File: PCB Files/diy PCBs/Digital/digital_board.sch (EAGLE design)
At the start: 18 parts

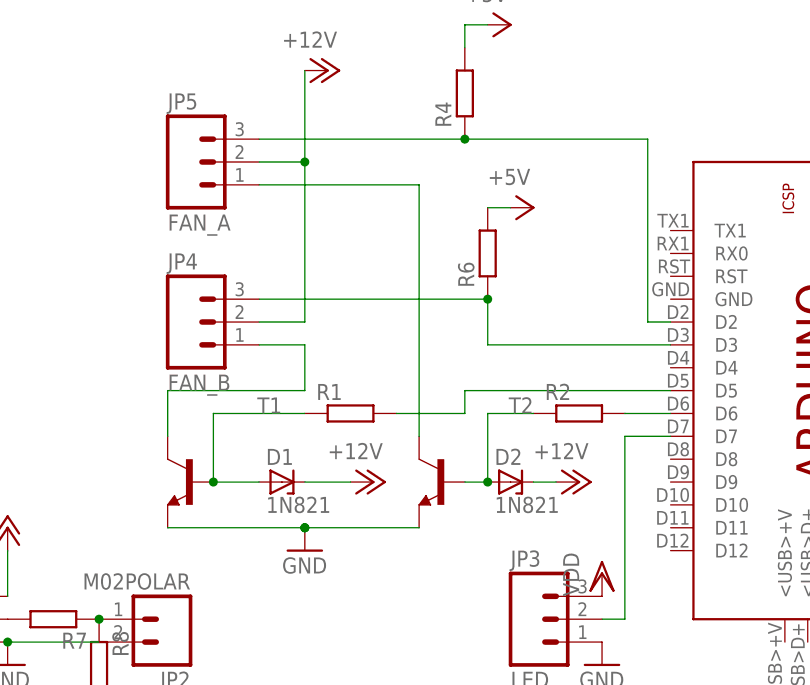
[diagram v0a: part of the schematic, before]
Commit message: made fixed a small bug and changed diode parameters
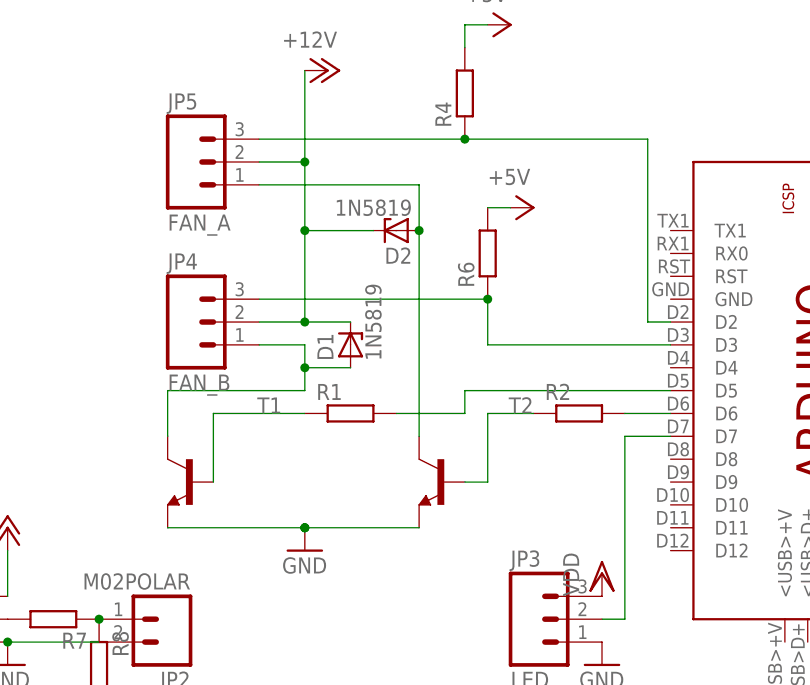
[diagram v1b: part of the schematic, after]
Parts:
- D1, D2: value 1N821 -> 1N5819
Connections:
- removed net N$6: D2.A, R2.1, T2.B
- new net N$2: R2.1
- net N$3: now also D1.A
- net N$4: now also D2.A
- net N$5: no longer D1.A
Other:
- moved on the sheet: D1, D2
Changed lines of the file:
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@@
 <part name="VDD1" library="supply1" deviceset="VDD" device=""/>
 <part name="VDD2" library="supply1" deviceset="VDD" device=""/>
-<part name="D1" library="diode" deviceset="1N821" device=""/>
-<part name="D2" library="diode" deviceset="1N821" device=""/>
-<part name="P+4" library="supply1" deviceset="+12V" device=""/>
-<part name="P+6" library="supply1" deviceset="+12V" device=""/>
+<part name="D1" library="diode" deviceset="1N821" device="" value="1N5819"/>
+<part name="D2" library="diode" deviceset="1N821" device="" value="1N5819"/>
 </parts>
 <sheets>
@@
 <instance part="VDD1" gate="G$1" x="0" y="25.4"/>
 <instance part="VDD2" gate="G$1" x="-27.94" y="-7.62" rot="R180"/>
-<instance part="D1" gate="1" x="-35.56" y="35.56"/>
-<instance part="D2" gate="1" x="-10.16" y="35.56"/>
-<instance part="P+4" gate="1" x="-25.4" y="35.56" rot="R270"/>
-<instance part="P+6" gate="1" x="-2.54" y="35.56" rot="R270"/>
+<instance part="D1" gate="1" x="-27.94" y="50.8" rot="R90"/>
+<instance part="D2" gate="1" x="-22.86" y="63.5" rot="R180"/>
 </instances>
 <busses>
@@
 <pinref part="T1" gate="G$1" pin="C"/>
 <wire x1="-38.1" y1="50.8" x2="-33.02" y2="50.8" width="0.1524" layer="91"/>
-<wire x1="-33.02" y1="50.8" x2="-33.02" y2="45.72" width="0.1524" layer="91"/>
+<wire x1="-33.02" y1="50.8" x2="-33.02" y2="48.26" width="0.1524" layer="91"/>
+<wire x1="-33.02" y1="48.26" x2="-33.02" y2="45.72" width="0.1524" layer="91"/>
 <wire x1="-33.02" y1="45.72" x2="-48.26" y2="45.72" width="0.1524" layer="91"/>
 <wire x1="-48.26" y1="45.72" x2="-48.26" y2="40.64" width="0.1524" layer="91"/>
+<pinref part="D1" gate="1" pin="A"/>
+<wire x1="-27.94" y1="48.26" x2="-33.02" y2="48.26" width="0.1524" layer="91"/>
+<junction x="-33.02" y="48.26"/>
 </segment>
 </net>
@@
 <pinref part="T2" gate="G$1" pin="C"/>
 <wire x1="-38.1" y1="68.58" x2="-20.32" y2="68.58" width="0.1524" layer="91"/>
-<wire x1="-20.32" y1="68.58" x2="-20.32" y2="40.64" width="0.1524" layer="91"/>
+<wire x1="-20.32" y1="68.58" x2="-20.32" y2="63.5" width="0.1524" layer="91"/>
+<pinref part="D2" gate="1" pin="A"/>
+<wire x1="-20.32" y1="63.5" x2="-20.32" y2="40.64" width="0.1524" layer="91"/>
+<junction x="-20.32" y="63.5"/>
 </segment>
 </net>
 <net name="+12V" class="0">
 <segment>
-<wire x1="-33.02" y1="53.34" x2="-33.02" y2="71.12" width="0.1524" layer="91"/>
+<wire x1="-33.02" y1="53.34" x2="-33.02" y2="63.5" width="0.1524" layer="91"/>
 <pinref part="P+1" gate="1" pin="+12V"/>
 <pinref part="JP5" gate="G$1" pin="2"/>
+<wire x1="-33.02" y1="63.5" x2="-33.02" y2="71.12" width="0.1524" layer="91"/>
 <wire x1="-33.02" y1="71.12" x2="-33.02" y2="81.28" width="0.1524" layer="91"/>
 <wire x1="-38.1" y1="71.12" x2="-33.02" y2="71.12" width="0.1524" layer="91"/>
@@
 <pinref part="JP4" gate="G$1" pin="2"/>
 <wire x1="-33.02" y1="53.34" x2="-38.1" y2="53.34" width="0.1524" layer="91"/>
+<pinref part="D1" gate="1" pin="C"/>
+<wire x1="-27.94" y1="53.34" x2="-33.02" y2="53.34" width="0.1524" layer="91"/>
+<pinref part="D2" gate="1" pin="C"/>
+<wire x1="-25.4" y1="63.5" x2="-33.02" y2="63.5" width="0.1524" layer="91"/>
+<junction x="-33.02" y="63.5"/>
+<junction x="-33.02" y="53.34"/>
 </segment>
 <segment>
@@
 <pinref part="JP6" gate="G$1" pin="4"/>
 <pinref part="P+5" gate="1" pin="+12V"/>
-</segment>
-<segment>
-<pinref part="D1" gate="1" pin="C"/>
-<pinref part="P+4" gate="1" pin="+12V"/>
-<wire x1="-33.02" y1="35.56" x2="-27.94" y2="35.56" width="0.1524" layer="91"/>
-</segment>
-<segment>
-<pinref part="D2" gate="1" pin="C"/>
-<pinref part="P+6" gate="1" pin="+12V"/>
-<wire x1="-5.08" y1="35.56" x2="-7.62" y2="35.56" width="0.1524" layer="91"/>
 </segment>
 </net>
@@
 <wire x1="-43.18" y1="43.18" x2="-43.18" y2="35.56" width="0.1524" layer="91"/>
 <pinref part="R1" gate="G$1" pin="1"/>
-<pinref part="D1" gate="1" pin="A"/>
-<junction x="-43.18" y="35.56"/>
-<wire x1="-43.18" y1="35.56" x2="-38.1" y2="35.56" width="0.1524" layer="91"/>
-</segment>
-</net>
-<net name="N$6" class="0">
-<segment>
-<pinref part="T2" gate="G$1" pin="B"/>
-<wire x1="-7.62" y1="43.18" x2="-12.7" y2="43.18" width="0.1524" layer="91"/>
-<wire x1="-12.7" y1="43.18" x2="-12.7" y2="35.56" width="0.1524" layer="91"/>
-<pinref part="R2" gate="G$1" pin="1"/>
-<pinref part="D2" gate="1" pin="A"/>
-<junction x="-12.7" y="35.56"/>
-<wire x1="-12.7" y1="35.56" x2="-15.24" y2="35.56" width="0.1524" layer="91"/>
 </segment>
 </net>
@@
 </segment>
 </net>
+<net name="N$2" class="0">
+<segment>
+<pinref part="R2" gate="G$1" pin="1"/>
+<wire x1="-7.62" y1="43.18" x2="-12.7" y2="43.18" width="0.1524" layer="91"/>
+<wire x1="-12.7" y1="43.18" x2="-12.7" y2="35.56" width="0.1524" layer="91"/>
+<wire x1="-12.7" y1="35.56" x2="-15.24" y2="35.56" width="0.1524" layer="91"/>
+</segment>
+</net>
